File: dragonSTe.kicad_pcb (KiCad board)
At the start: 4 copper layers, 329 parts, among them J13 FDD Power, J2 MIDI OUT, J3 MIDI IN, J4 DB25_Socket, J5 DB25_Pins, J6 Keyboard, J7 Internal FDD, J8 JOY0, J9 JOY1, Q1 2N3904, Q10 2N3904, Q2 2N3904, Q3 2N3904, Q4 2N3904, Q5 2N3904, Q6 2N3904, Q7 2N3904, Q8 2N3904, Q9 2N3904, SW1 RESET, U1 68000, U10 MC68901, U13 74HCT14D, U15 74HC86, U18 74HC74, U19 74HC244, U2 27C010, U20 74HC245, U21 74HC74, U22 74HS05, U23 74HC374, U24 74HC374, U25 74HC244, U26 74HC244, U27 74HC373, U28 74HC244, U29 DAC0802, U3 27C010, U30 LF347DT, U31 DAC0802, U32 LF347DT, U33 LM78L82, U34 LMC1992, U37 DMA, U38 WD1772, U39 STB, U4 74HC74, U40 GST_SHIFTER, U42 GST_MCU, U43 74HC244, U44 74HC86, U45 74HCT14D, U5 LM555xM, U6 74HS05, U7 MC6850, U8 MC6850, U9 YM2149, X1 8.010613MHz

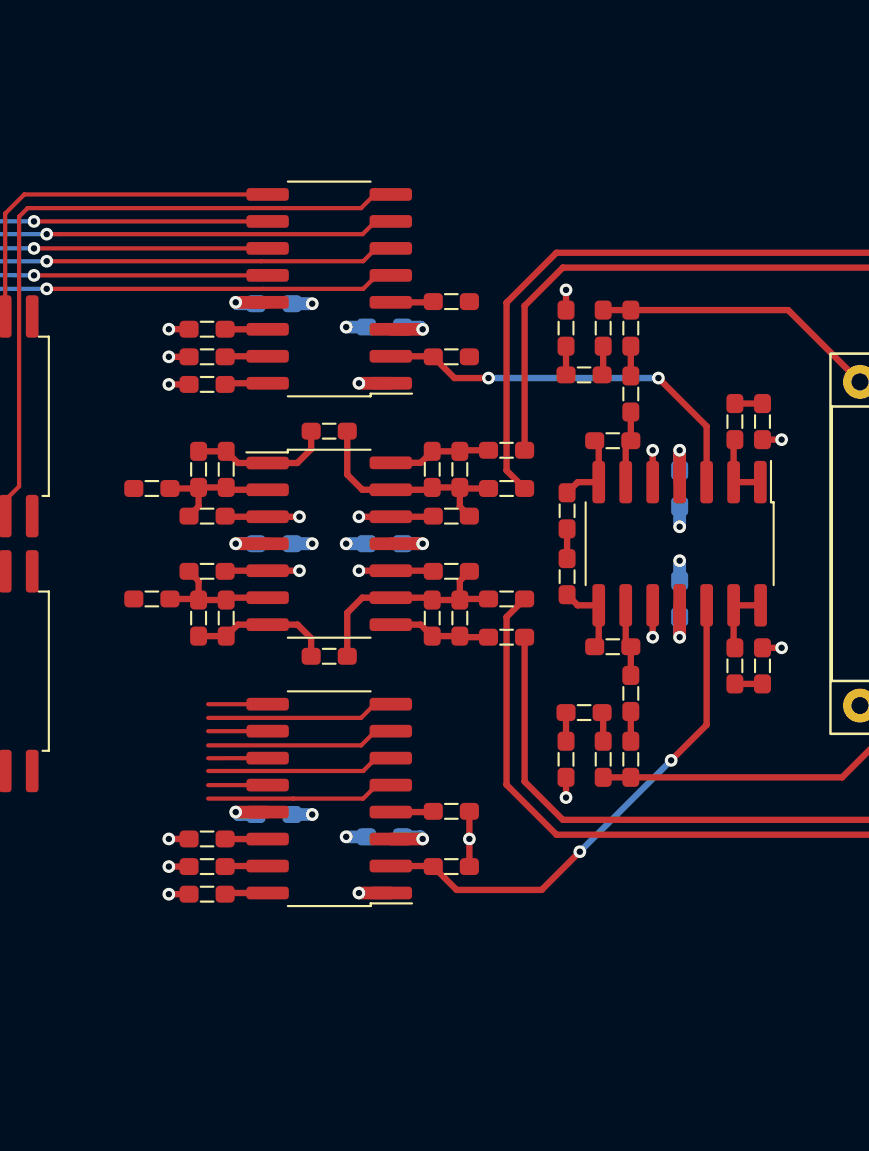
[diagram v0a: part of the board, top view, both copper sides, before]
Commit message: motherboard: Added the Butterworth filters for the audio paths so they work correctly
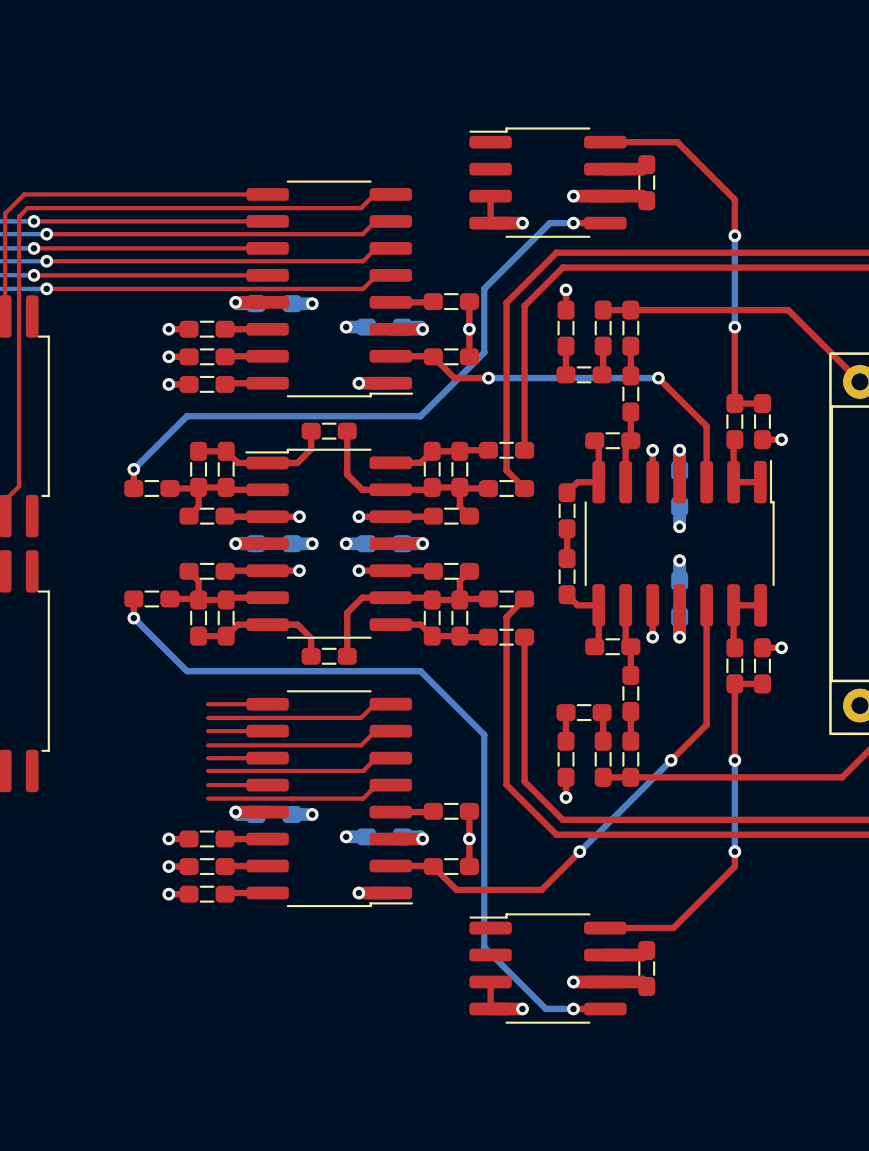
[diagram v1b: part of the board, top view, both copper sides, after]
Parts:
- added C114: 100n, rhais_rcl:C0603, F.Cu at (79.7, 38.0)
- added C115: 100n, rhais_rcl:C0603, F.Cu at (79.7, 75.0)
- added U46: TLC04, rhais_package-smd:SO-8_3.9x4.9mm_P1.27mm, F.Cu at (75.0, 38.0)
- added U47: TLC04, rhais_package-smd:SO-8_3.9x4.9mm_P1.27mm, F.Cu at (75.0, 75.0)
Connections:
- R55 pad 2: unconnected-(R55-Pad2) -> Net-(U46-OUT)
- R60 pad 2: unconnected-(R60-Pad2) -> Net-(U47-OUT)
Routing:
- net Net-(U47-OUT): track 0.00 -> 36.6 mm, vias 0 -> 2
- net Net-(U46-OUT): track 0.00 -> 29.7 mm, vias 0 -> 2
- net Net-(U46-IN): track 1.30 -> 18.1 mm, vias 0 -> 2
- net Net-(U47-IN): track 1.30 -> 17.2 mm, vias 0 -> 2
- net GND: track 51.5 -> 64.1 mm, vias 38 -> 42
- net /DAC + Joysticks/+5VA: track 11.9 -> 18.6 mm, vias 6 -> 7

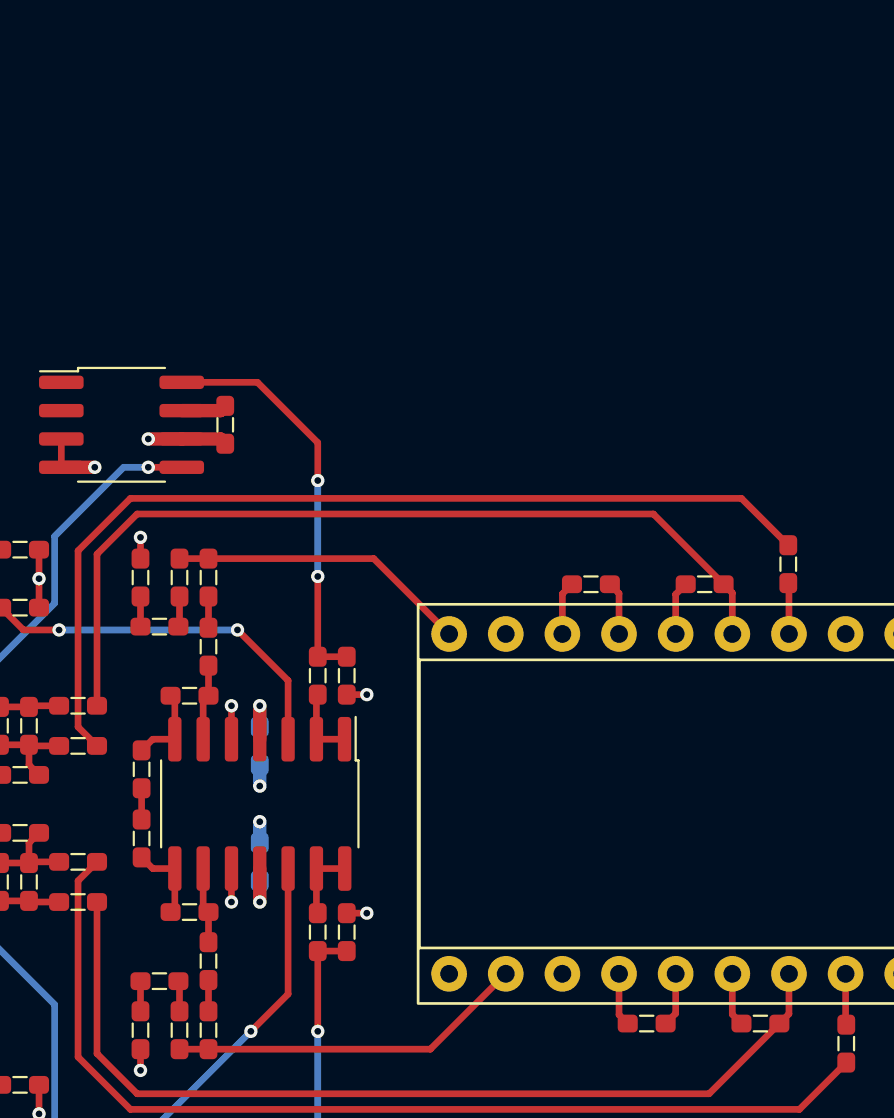
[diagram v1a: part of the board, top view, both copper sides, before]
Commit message: motherboard: Added the main RCA-based audio out connections, completing the audio section
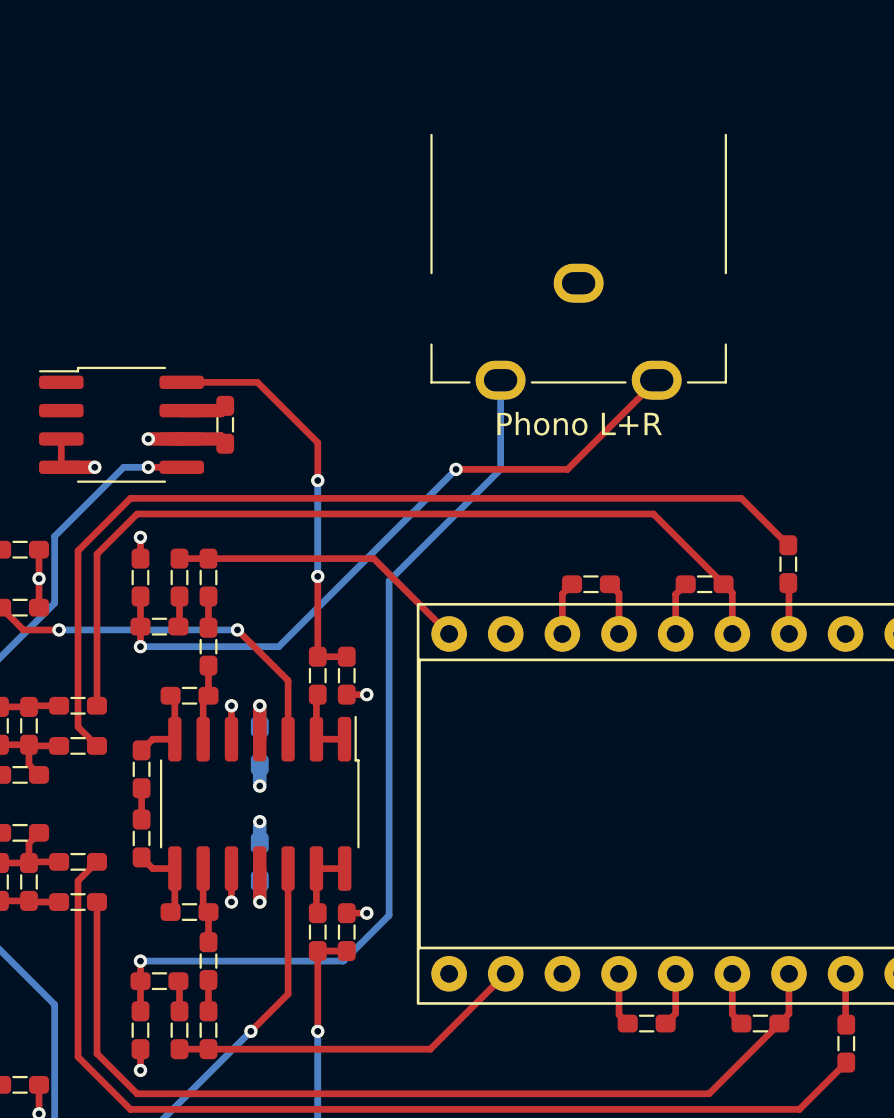
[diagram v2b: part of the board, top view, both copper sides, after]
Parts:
- added J10: Phono L+R, rhais_connector-multicomp:PSG01550, F.Cu at (95.5, 30.0)
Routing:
- net Net-(J10-IN2): track 1.35 -> 40.3 mm, vias 0 -> 1
- net Net-(J10-IN1): track 1.35 -> 30.3 mm, vias 0 -> 2

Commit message: motherboard: Reorganised a bit to start bringing the I/O interfaces together and setting their routing into place a bit
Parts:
- moved U45 123.1 mm to (353.0, 138.0)
- moved C20 106.3 mm to (211.7, 153.6)
- moved C21 106.3 mm to (211.7, 155.9)
- moved C22 106.3 mm to (211.7, 158.2)
- moved C23 106.3 mm to (211.7, 160.6)
- moved Q10 106.3 mm to (183.1, 176.9)
- moved R3 106.3 mm to (211.7, 170.0)
- moved R4 106.3 mm to (211.7, 172.3)
- moved C1 106.3 mm to (203.4, 153.6)
- moved C11 106.3 mm to (207.6, 153.6)
- moved C12 106.3 mm to (207.6, 155.9)
- moved C13 106.3 mm to (207.6, 158.2)
- moved C16 106.3 mm to (207.6, 165.3)
- moved C17 106.3 mm to (207.6, 167.7)
- moved C2 106.3 mm to (203.4, 155.9)
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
